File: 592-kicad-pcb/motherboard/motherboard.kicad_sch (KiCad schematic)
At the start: 1 part, among them U12 NUCLEO144-F746ZG

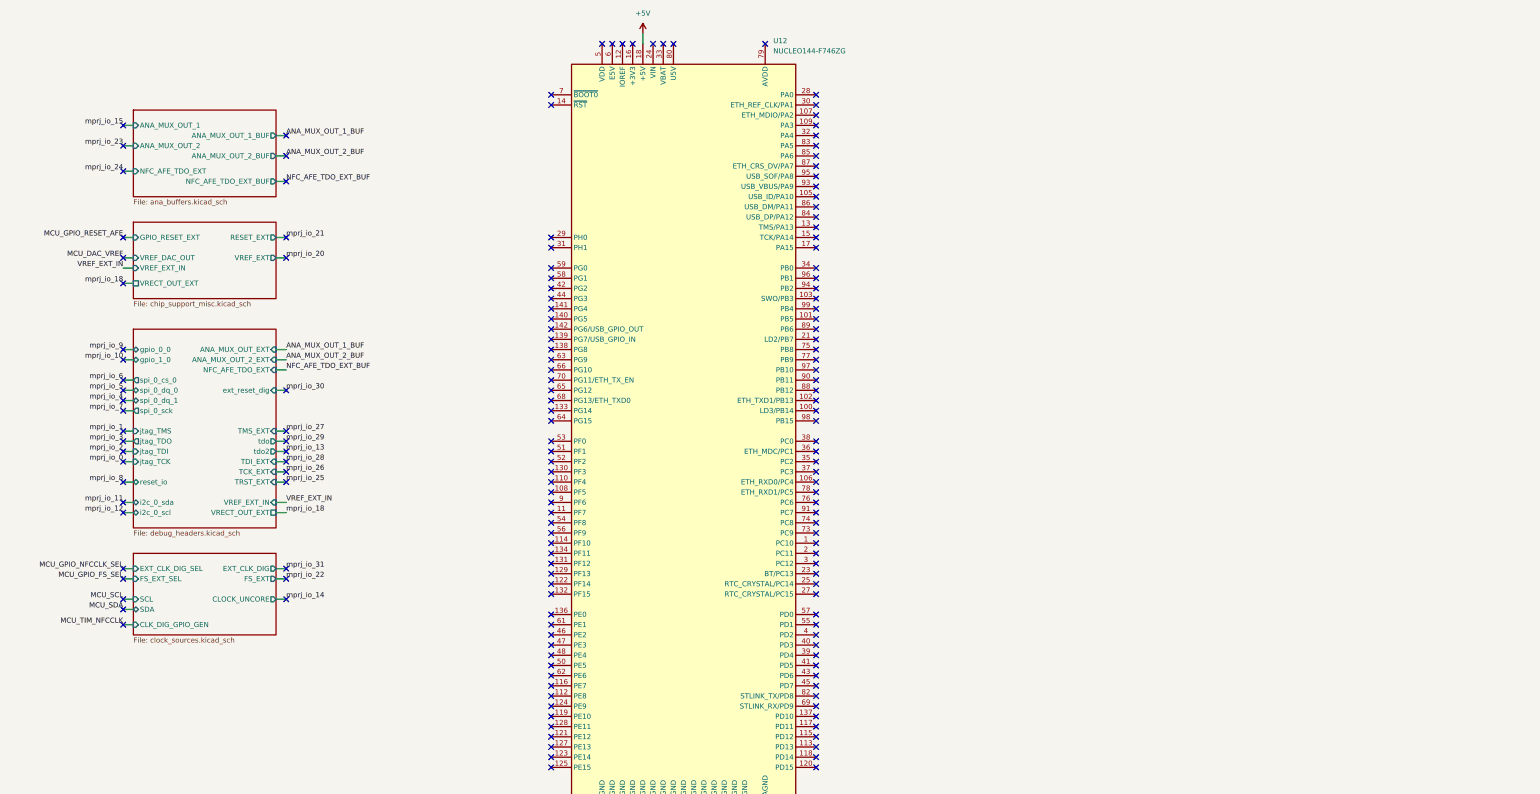
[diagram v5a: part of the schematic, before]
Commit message: update motheboard schems to include conn
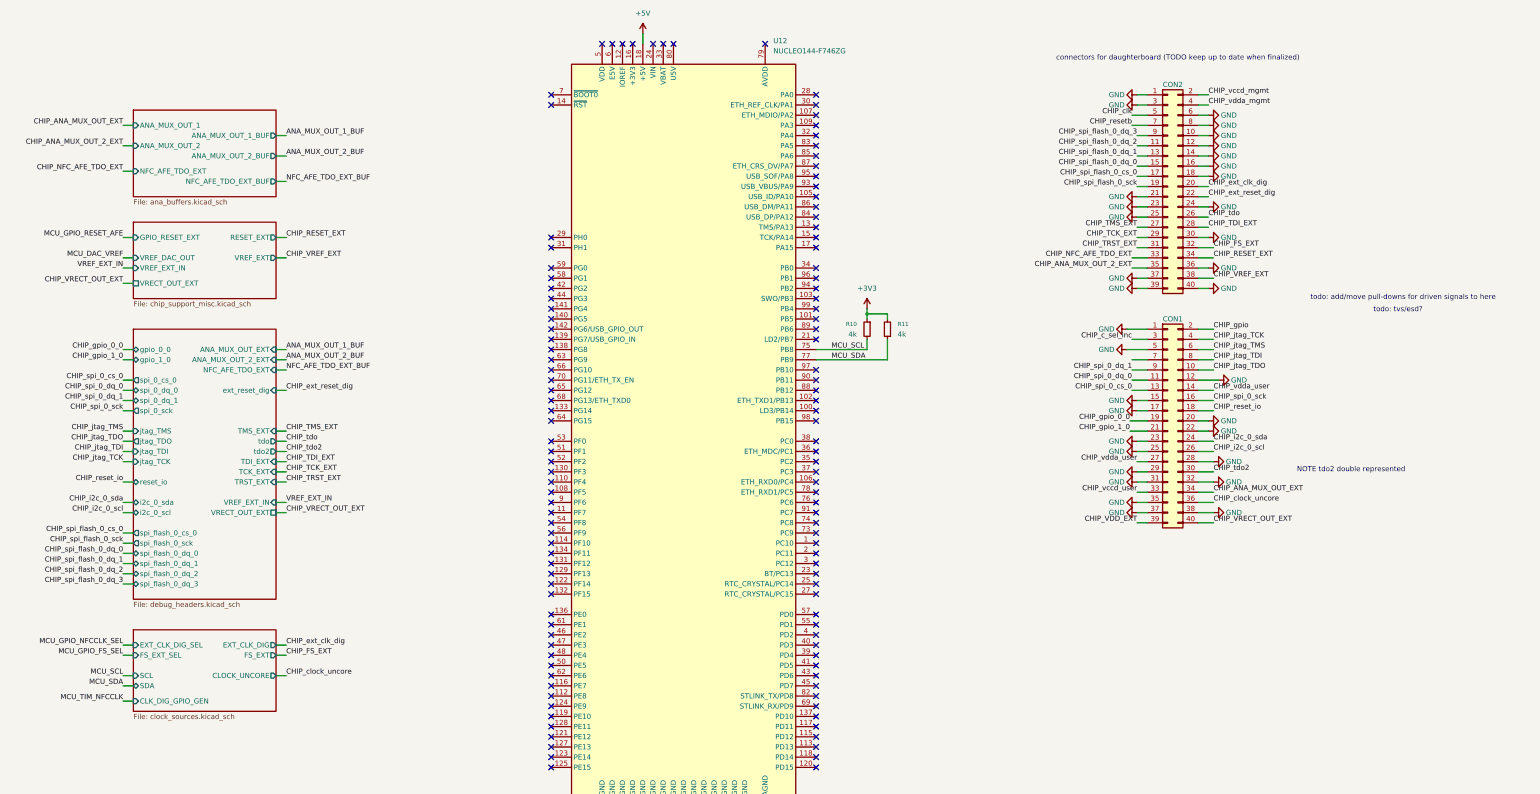
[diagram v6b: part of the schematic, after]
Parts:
- added CON1, CON2: ~, TinyTapeout:FH-00148_PinSocket_2x20_P2.54mm, symbol Connector_Generic:Conn_02x20_Odd_Even
- added R10, R11: 4k, symbol Device:R_Small
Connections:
- net GND: now also CON1.1 (Pin_1), CON1.12 (Pin_12), CON1.15 (Pin_15), CON1.17 (Pin_17), CON1.20 (Pin_20), CON1.22 (Pin_22), CON1.23 (Pin_23), CON1.25 (Pin_25), CON1.28 (Pin_28), CON1.29 (Pin_29), CON1.31 (Pin_31), CON1.32 (Pin_32), CON1.35 (Pin_35), CON1.37 (Pin_37), CON1.38 (Pin_38), CON1.5 (Pin_5), CON2.1 (Pin_1), CON2.10 (Pin_10), CON2.12 (Pin_12), CON2.14 (Pin_14), CON2.16 (Pin_16), CON2.18 (Pin_18), CON2.21 (Pin_21), CON2.23 (Pin_23), CON2.24 (Pin_24), CON2.25 (Pin_25), CON2.3 (Pin_3), CON2.30 (Pin_30), CON2.36 (Pin_36), CON2.37 (Pin_37), CON2.39 (Pin_39), CON2.40 (Pin_40), CON2.6 (Pin_6), CON2.8 (Pin_8)
- net MCU_SCL: now also U12.75 (PB8), R10.2
- net MCU_SDA: now also U12.77 (PB9), R11.1
- new net +3V3: R10.1, R11.2
- new net CHIP_ANA_MUX_OUT_2_EXT: CON2.35 (Pin_35)
- new net CHIP_ANA_MUX_OUT_EXT: CON1.34 (Pin_34)
- new net CHIP_FS_EXT: CON2.32 (Pin_32)
- new net CHIP_NFC_AFE_TDO_EXT: CON2.33 (Pin_33)
- new net CHIP_RESET_EXT: CON2.34 (Pin_34)
- new net CHIP_TCK_EXT: CON2.29 (Pin_29)
- new net CHIP_TDI_EXT: CON2.28 (Pin_28)
- new net CHIP_TMS_EXT: CON2.27 (Pin_27)
- new net CHIP_TRST_EXT: CON2.31 (Pin_31)
- new net CHIP_VDD_EXT: CON1.39 (Pin_39)
- new net CHIP_VRECT_OUT_EXT: CON1.40 (Pin_40)
- new net CHIP_VREF_EXT: CON2.38 (Pin_38)
- new net CHIP_c_sel_inc: CON1.3 (Pin_3)
- new net CHIP_clk: CON2.5 (Pin_5)
- new net CHIP_clock_uncore: CON1.36 (Pin_36)
- new net CHIP_ext_clk_dig: CON2.20 (Pin_20)
- new net CHIP_ext_reset_dig: CON2.22 (Pin_22)
- new net CHIP_gpio: CON1.2 (Pin_2)
- new net CHIP_gpio_0_0: CON1.19 (Pin_19)
- new net CHIP_gpio_1_0: CON1.21 (Pin_21)
- new net CHIP_i2c_0_scl: CON1.26 (Pin_26)
- new net CHIP_i2c_0_sda: CON1.24 (Pin_24)
- new net CHIP_jtag_TCK: CON1.4 (Pin_4)
- new net CHIP_jtag_TDI: CON1.8 (Pin_8)
- new net CHIP_jtag_TDO: CON1.10 (Pin_10)
- new net CHIP_jtag_TMS: CON1.6 (Pin_6)
- new net CHIP_reset_io: CON1.18 (Pin_18)
- new net CHIP_resetb: CON2.7 (Pin_7)
- new net CHIP_spi_0_cs_0: CON1.13 (Pin_13)
- new net CHIP_spi_0_dq_0: CON1.11 (Pin_11)
- new net CHIP_spi_0_dq_1: CON1.9 (Pin_9)
- new net CHIP_spi_0_sck: CON1.16 (Pin_16)
- new net CHIP_spi_flash_0_cs_0: CON2.17 (Pin_17)
- new net CHIP_spi_flash_0_dq_0: CON2.15 (Pin_15)
- new net CHIP_spi_flash_0_dq_1: CON2.13 (Pin_13)
- new net CHIP_spi_flash_0_dq_2: CON2.11 (Pin_11)
- new net CHIP_spi_flash_0_dq_3: CON2.9 (Pin_9)
- new net CHIP_spi_flash_0_sck: CON2.19 (Pin_19)
- new net CHIP_tdo: CON2.26 (Pin_26)
- new net CHIP_tdo2: CON1.30 (Pin_30)
- new net CHIP_vccd_mgmt: CON2.2 (Pin_2)
- new net CHIP_vccd_user: CON1.33 (Pin_33)
- new net CHIP_vdda_mgmt: CON2.4 (Pin_4)
- new net CHIP_vdda_user: CON1.14 (Pin_14), CON1.27 (Pin_27)
- no-connect marks 163 -> 122
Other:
- sheet debug_headers ports: added spi_flash_0_cs_0, spi_flash_0_dq_0, spi_flash_0_dq_1, spi_flash_0_dq_2, spi_flash_0_dq_3, spi_flash_0_sck; removed none
- note added: "NOTE tdo2 double represented"
- note added: "connectors for daughterboard (TODO keep up to date when finalized)"
- note added: "todo: add/move pull-downs for driven signals to here"
- note added: "todo: tvs/esd?"

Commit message: in-class work at schems
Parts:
- removed R10, R11: 4k, symbol Device:R_Small
- removed U12: NUCLEO144-F746ZG, Module:ST_Morpho_Connector_144_STLink, symbol MCU_Module:NUCLEO144-F746ZG
- added R12, R13: 4k, symbol Device:R_Small
- added U10: NUCLEO144-F746ZG, Module:ST_Morpho_Connector_144_STLink, symbol MCU_Module:NUCLEO144-F746ZG
- added U7: STM32H563ZITx, Package_QFP:LQFP-144_20x20mm_P0.5mm, symbol MCU_ST_STM32H5:STM32H563ZITx
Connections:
- net +3V3: now also R12.1, R13.2
- net +5V: now also U10.18 (+5V)
- net GND: now also U10.104 (AGND), U10.111 (GND), U10.126 (GND), U10.135 (GND), U10.143 (GND), U10.144 (GND), U10.19 (GND), U10.20 (GND), U10.22 (GND), U10.49 (GND), U10.60 (GND), U10.71 (GND), U10.72 (GND), U10.8 (GND), U10.81 (GND), U10.92 (GND)
- net MCU_SCL: now also R12.2, U10.75 (PB8)
- net MCU_SDA: now also R13.1, U10.77 (PB9)
- new net: U7.107 (VSS), U7.120 (VSS), U7.130 (VSS), U7.143 (VSS), U7.16 (VSS), U7.38 (VSS), U7.51 (VSS), U7.61 (VSS), U7.71 (VSS), U7.83 (VSS), U7.94 (VSS)
- new net EN_VOUT1: U10.52 (PF2)
- new net EN_VOUT2: U10.47 (PE3)
- new net I2C4_SCL: U10.115 (PD12)
- new net I2C4_SDA: U10.113 (PD13)
- new net SPI4_CS: U10.128 (PE11)
- new net SPI4_MISO: U10.127 (PE13)
- new net SPI4_MOSI: U10.123 (PE14)
- new net SPI4_SCK: U10.121 (PE12)
- new net SPI5_CS: U10.9 (PF6)
- new net SPI5_MISO: U10.54 (PF8)
- new net SPI5_MOSI: U10.56 (PF9)
- new net SPI5_SCK: U10.11 (PF7)
- new net TIM3_CH2: U10.101 (PB5)
- new net UART8_RX: U10.136 (PE0)
- new net UART8_TX: U10.61 (PE1)
- new net gpio: U10.137 (PD10)
- new net mprj_io[0]: U10.65 (PG12)
- new net mprj_io[10]: U10.59 (PG0)
- new net mprj_io[11]: U10.58 (PG1)
- new net mprj_io[12]: U10.45 (PD7)
- new net mprj_io[13]: U10.44 (PG3)
- new net mprj_io[14]: U10.43 (PD6)
- new net mprj_io[15]: U10.42 (PG2)
- new net mprj_io[16]: U10.41 (PD5)
- new net mprj_io[17]: U10.40 (PD3)
- new net mprj_io[18]: U10.39 (PD4)
- new net mprj_io[19]: U10.38 (PC0)
- new net mprj_io[20]: U10.37 (PC3)
- new net mprj_io[21]: U10.35 (PC2)
- new net mprj_io[22]: U10.32 (PA4)
- new net mprj_io[23]: U10.28 (PA0)
- new net mprj_io[24]: U10.17 (PA15)
- new net mprj_io[25]: U10.1 (PC10)
- new net mprj_io[26]: U10.2 (PC11)
- new net mprj_io[27]: U10.4 (PD2)
- new net mprj_io[28]: U10.73 (PC9)
- new net mprj_io[29]: U10.74 (PC8)
- new net mprj_io[31]: U10.76 (PC6)
- new net mprj_io[33]: U10.88 (PB12)
- new net mprj_io[34]: U10.89 (PB6)
- new net mprj_io[35]: U10.94 (PB2)
- new net mprj_io[36]: U10.96 (PB1)
- new net mprj_io[37]: U10.98 (PB15)
- new net mprj_io[7]: U10.66 (PG10)
- new net mprj_io[8]: U10.64 (PG15)
- new net mprj_io[9]: U10.63 (PG9)
- new net ~{MR}: U10.3 (PC12)
- no-connect marks 122 -> 39
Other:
- note added: "TODO: use new zio connector pinout"

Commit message: clean up some pull up/downs
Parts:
- added R20, R25: 4k, symbol Device:R_Small
- added R21, R22: 100k, symbol Device:R_Small
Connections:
- net +3V3: now also R20.1, R21.1, R22.1, R25.2
- net CHIP_i2c_0_scl: now also R25.1
- net CHIP_i2c_0_sda: now also R20.2
- net CHIP_spi_0_cs_0: now also R22.2
- net CHIP_spi_flash_0_cs_0: now also R21.2
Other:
- note added: "TODO: use new zio connector pinout?"
- note added: "add pull-downs where applicable for inputs to chips from the NFC chip consider just using GPIO PDN on STM. need to add discretes for other chips"
- note added: "only including pull-ups here for: a) I2C (needs ~2k usually) b) CS for SPI (assume that peripherals could be in a bad state w/out chip)"
- note removed: "NOTE tdo2 double represented"
- note removed: "TODO: use new zio connector pinout"
- note removed: "todo: add/move pull-downs for driven signals to here"
- note removed: "todo: tvs/esd?"
- moved on the sheet: CON1, CON2, R12, R13, U10, U7
